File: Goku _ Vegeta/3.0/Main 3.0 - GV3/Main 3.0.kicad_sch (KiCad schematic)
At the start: 28 parts, among them J11 Motor Driver Inputs, J12 OpenMV H7, J13 Conn_01x04_Male, J15 Motor Driver 1 Power, J16 Motor Driver 2 Power, J23 Line PCB 2, J24 B3B-XH-A(LF)(SN), J25 Conn_01x02_Male, J5 XT60-M, J6 Voltmeter, J7 XT60-M, J8 XT60-M, J9 Line PCB 1, U1 DC-DC_Buck_Converter_7-24V_to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, U2 DEV-16771, U4 Adafruit_BNO055_STEMMA_QT

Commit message: Line 3.0 SCH 1st draft done + started working on SCH for main 3.0
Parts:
- removed C1, C3, C4: 10UF, Capacitor_SMD:C_0805_2012Metric, symbol Device:C_Small
- removed J11: Motor Driver Inputs, Box IDC header 2x5:Box IDC header 2x5, symbol Box IDC header 2x5:2-1761603-3
- removed J12: OpenMV H7, Box IDC header 2x3:Box IDC header 2x3, symbol Box IDC header 2x3:2-1761679-1
- removed J15: Motor Driver 1 Power, 5mm Pitch 2-Pin Screw Terminal Block:5mm Pitch 2-Pin Screw Terminal Block, symbol 5mm Pitch 2-Pin Screw Terminal Block:691137710002
- removed J16: Motor Driver 2 Power, 5mm Pitch 2-Pin Screw Terminal Block:5mm Pitch 2-Pin Screw Terminal Block, symbol 5mm Pitch 2-Pin Screw Terminal Block:691137710002
- removed J23: Line PCB 2, Box IDC header 2x3:Box IDC header 2x3, symbol Box IDC header 2x3:2-1761679-1
- removed J24: B3B-XH-A(LF)(SN), JST_B3B-XH-A(LF)(SN), symbol B3B-XH-A_LF__SN_:B3B-XH-A(LF)(SN)
- removed J5, J7, J8: XT60-M, XT60-M:XT60-M, symbol XT60-M:XT60-M
- removed J9: Line PCB 1, Box IDC header 2x3:Box IDC header 2x3, symbol Box IDC header 2x3:2-1761679-1
- removed U1: DC-DC_Buck_Converter_7-24V_to_5V_4A, 2.3 PCBs:DC-DC_Buck_Converter_7-24V_to_5V_4A, symbol DC-DC Buck Converter 7-24V to 5V 4A:DC-DC_Buck_Converter_7-24V_to_5V_4A
- removed U2: DEV-16771, MODULE_DEV-16771, symbol DEV-16771:DEV-16771
- added C1, C2: 10uF, Capacitor_SMD:C_0805_2012Metric, symbol Device:C_Polarized_Small
- added C3, C4: 0.1uF, Capacitor_SMD:C_0805_2012Metric, symbol Device:C_Polarized_Small
- added C5, C6: 3.3nF, Capacitor_SMD:C_0805_2012Metric, symbol Device:C_Polarized_Small
- added C7, C8: 22uF, Capacitor_SMD:C_0805_2012Metric, symbol Device:C_Polarized_Small
- added D1: LED, symbol Device:LED
- added D2, D3: STTH2002G-TR, Package_TO_SOT_SMD:TO-263-2, symbol Diode:STTH2002G
- added J1: Battery Buzzer 1, Connector_PinSocket_2.54mm:PinSocket_1x08_P2.54mm_Vertical, symbol Connector:Conn_01x08_Pin
- added J10: Power Switch, Connector_AMASS:AMASS_XT60-F_1x02_P7.20mm_Vertical, symbol Connector_Generic:Conn_01x02
- added J11: LEFT HEADERS, Connector_PinHeader_2.54mm:PinHeader_1x24_P2.54mm_Vertical, symbol Connector:Conn_01x24_Female
- added J14: RIGHT HEADERS, Connector_PinHeader_2.54mm:PinHeader_1x24_P2.54mm_Vertical, symbol Connector:Conn_01x24_Female
- added J2: Battery Buzzer 2, Connector_PinSocket_2.54mm:PinSocket_1x08_P2.54mm_Vertical, symbol Connector:Conn_01x08_Pin
- added J3: Battery Balance 1, Connector_JST:JST_XH_B3B-XH-A_1x03_P2.50mm_Vertical, symbol Connector:Conn_01x03_Socket
- added J4: Battery Balance 2, Connector_JST:JST_XH_B3B-XH-A_1x03_P2.50mm_Vertical, symbol Connector:Conn_01x03_Socket
- added J5: Battery 1, Connectors:DEANS, symbol Connector_Generic:Conn_01x02
- added J7: Battery 2, Connectors:DEANS, symbol Connector_Generic:Conn_01x02
- added J8: B-B PWR, Connector_AMASS:AMASS_XT60-F_1x02_P7.20mm_Vertical, symbol Connector_Generic:Conn_01x02
- added J9: I2C TO SLAVE, Connector_JST:JST_XH_B4B-XH-AM_1x04_P2.50mm_Vertical, symbol Connector:Conn_01x04_Male
- added L1, L2: 2.2uH, symbol Device:L
- added Q1: Q_Photo_NPN, symbol Device:Q_Photo_NPN
- added R1, R2: 100K, Resistor_SMD:R_0805_2012Metric, symbol Device:R_Small
- added R3: 95R, Resistor_SMD:R_0805_2012Metric, symbol Device:R_Small
- added R4, R5: 10K, Resistor_SMD:R_0805_2012Metric, symbol Device:R_Small
- added SW1: SW_DIP_x04, Button_Switch_THT:SW_DIP_SPSTx04_Slide_9.78x12.34mm_W7.62mm_P2.54mm, symbol Switch:SW_DIP_x04
- added U1: DEV-16771, DEV-16771:MODULE_DEV-16771, symbol DEV-16771:DEV-16771
- added U2: TPS62132, Package_DFN_QFN:VQFN-16-1EP_3x3mm_P0.5mm_EP1.68x1.68mm_ThermalVias, symbol Regulator_Switching:TPS62132
- added U3: TPS62133, Package_DFN_QFN:VQFN-16-1EP_3x3mm_P0.5mm_EP1.68x1.68mm_ThermalVias, symbol Regulator_Switching:TPS62133
- J13: value Conn_01x04_Male -> UART TO CAM; footprint (none) -> Connector_JST:JST_XH_B4B-XH-AM_1x04_P2.50mm_Vertical
- J25: footprint (none) -> Connector_JST:JST_XH_B2B-XH-A_1x02_P2.50mm_Vertical
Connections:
- net +15V: now also D2.3 (A), D3.3 (A), J10.2 (Pin_2), J8.1 (Pin_1)
- net +5V: now also C8.1, J14.1 (Pin_1), L2.2, Q1.1 (C), R2.2, R3.1, U1.5V, U1.VIN, U3.14 (VOS)
- net GND: now also J13.4 (Pin_4), C1.2, C3.2, C5.1, C7.2, C8.2, D1.1 (K), J11.1 (Pin_1), J14.15 (Pin_15), J14.2 (Pin_2), J7.1 (Pin_1), J8.2 (Pin_2), J9.4 (Pin_4), R4.2, R5.2, U1.GND1 (GND), U1.GND2 (GND__1), U1.GND3 (GND__2), U1.GND4 (GND__3), U1.GND5 (GND__4), U1.USB_GND1 (USB_GND), U1.USB_GND2 (USB_GND__1), U2.15 (PGND), U2.16 (PGND), U2.17 (EP), U2.5 (FB), U2.6 (AGND), U2.7 (FSW), U2.8 (DEF), U3.15 (PGND), U3.16 (PGND), U3.17 (EP), U3.5 (FB); no longer J13.2 (Pin_2)
- net LOGIC_SWTICH: now also R5.1
- net RST renamed 33
- net 33: now also J14.24 (Pin_24), U1.33 (MCLK2)
- net RX renamed 0
- net 0: now also J13.3 (Pin_3), J11.2 (Pin_2), U1.0 (RX1)
- net SCL renamed 19
- net 19: now also J14.8 (Pin_8), J9.3 (Pin_3), U1.19 (A5); no longer J13.3 (Pin_3)
- net SDA renamed 18
- net 18: now also J14.9 (Pin_9), J9.2 (Pin_2), U1.18 (A4); no longer J13.4 (Pin_4)
- net TX renamed 1
- net 1: now also J13.2 (Pin_2), J11.3 (Pin_3), U1.1 (TX1)
- new net: L1.1, U2.1 (SW), U2.2 (SW), U2.3 (SW)
- new net: C1.1, C3.1, D2.2 (K), U2.10 (AVIN), U2.11 (PVIN), U2.12 (PVIN), U2.13 (EN)
- new net: R1.1, U2.4 (PG)
- new net: C5.2, U2.9 (SS/TR)
- new net: L2.1, U3.1 (SW), U3.2 (SW), U3.3 (SW)
- new net: D1.2 (A), R3.2
- new net: J5.1 (Pin_1), J7.2 (Pin_2)
- new net: J1.3 (Pin_3), J3.1 (Pin_1)
- new net: J1.2 (Pin_2), J3.2 (Pin_2)
- new net: J1.1 (Pin_1), J3.3 (Pin_3)
- new net: C2.1, C4.1, D3.2 (K), U3.10 (AVIN), U3.11 (PVIN), U3.12 (PVIN), U3.13 (EN)
- new net: R2.1, U3.4 (PG)
- new net: C2.2, C4.2, C6.1, U3.6 (AGND), U3.7 (FSW), U3.8 (DEF)
- new net: C6.2, U3.9 (SS/TR)
- new net: J10.1 (Pin_1), J5.2 (Pin_2)
- new net: J2.1 (Pin_1), J4.3 (Pin_3)
- new net: J2.2 (Pin_2), J4.2 (Pin_2)
- new net: J2.3 (Pin_3), J4.1 (Pin_1)
- new net +3V3: C7.1, J11.15 (Pin_15), J14.3 (Pin_3), L1.2, R1.2, SW1.1, SW1.2, SW1.3, SW1.4, U2.14 (VOS)
- new net 10: J11.12 (Pin_12), U1.10 (CS1)
- new net 11: J11.13 (Pin_13), U1.11 (MOSI)
- new net 12: J11.14 (Pin_14), U1.12 (MISO)
- new net 13: J14.14 (Pin_14), U1.13 (SCK)
- new net 14: J14.13 (Pin_13), U1.14 (A0)
- new net 15: J14.12 (Pin_12), U1.15 (A1)
- new net 16: J14.11 (Pin_11), U1.16 (A2)
- new net 17: J14.10 (Pin_10), U1.17 (A3)
- new net 2: J11.4 (Pin_4), U1.2 (OUT2)
- new net 20: J14.7 (Pin_7), U1.20 (A6)
- new net 21: J14.6 (Pin_6), U1.21 (A7)
- new net 22: J14.5 (Pin_5), U1.22 (A8)
- new net 23: J14.4 (Pin_4), U1.23 (A9)
- new net 24: J11.16 (Pin_16), Q1.2 (E), R4.1, U1.24 (A10)
- new net 25: J11.17 (Pin_17), U1.25 (A11)
- new net 26: J11.18 (Pin_18), U1.26 (A12)
- new net 27: J11.19 (Pin_19), U1.27 (A13)
- new net 28: J11.20 (Pin_20), SW1.6, U1.28 (RX7)
- new net 29: J11.21 (Pin_21), SW1.5, U1.29 (TX7)
- new net 3: J11.5 (Pin_5), U1.3 (LRCLK2)
- new net 30: J11.22 (Pin_22), U1.30 (CRX3)
- new net 31: J11.23 (Pin_23), U1.31 (CTX3)
- new net 32: J11.24 (Pin_24), J9.1 (Pin_1), U1.32 (OUT1B)
- new net 34: J14.23 (Pin_23), U1.34 (RX8)
- new net 35: J14.22 (Pin_22), U1.35 (TX8)
- new net 36: J14.21 (Pin_21), U1.36 (CS2)
- new net 37: J14.20 (Pin_20), U1.37 (CS3)
- new net 38: J14.19 (Pin_19), U1.38 (A14)
- new net 39: J14.18 (Pin_18), U1.39 (A15)
- new net 4: J11.6 (Pin_6), U1.4 (BCLK2)
- new net 40: J14.17 (Pin_17), U1.40 (A16)
- new net 41: J14.16 (Pin_16), U1.41 (A17)
- new net 5: J11.7 (Pin_7), U1.5 (IN2)
- new net 6: J11.8 (Pin_8), U1.6 (OUT1D)
- new net 7: J11.9 (Pin_9), SW1.8, U1.7 (RX2)
- new net 8: J11.10 (Pin_10), SW1.7, U1.8 (TX2)
- new net 9: J11.11 (Pin_11), U1.9 (OUT1C)
- no-connect marks 7 -> 29
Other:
- note added: "3V3 POWER RAIL - LEDs and Phototransistors"
- note added: "5V POWER RAIL - Microcontroller"
- note added: "LINE BREAK CIRCUIT"
- note added: "MCU"
- note added: "POWER SUPPLY"
- note added: "double check polarity of connections"
- note removed: "Battery 1"
- note removed: "Battery 2"
- note removed: "Power Switch"
- moved on the sheet: J6, R13, R14, TP1, TP2, TP3, TP4, TP5, TP6

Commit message: LINE 3.0 Update
-Updated to have caps on power rails
-imrpoves tolerance of 100uf capacitor
-main power cable went from xt60 to xt30
- remove outer wheel guard
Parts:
- removed C3, C4: 0.1uF, Capacitor_SMD:C_0805_2012Metric, symbol Device:C_Polarized_Small
- removed C5, C6: 3.3nF, Capacitor_SMD:C_0805_2012Metric, symbol Device:C_Polarized_Small
- removed C7, C8: 22uF, Capacitor_SMD:C_0805_2012Metric, symbol Device:C_Polarized_Small
- removed D2, D3: STTH2002G-TR, Package_TO_SOT_SMD:TO-263-2, symbol Diode:STTH2002G
- removed J10: Power Switch, Connector_AMASS:AMASS_XT60-F_1x02_P7.20mm_Vertical, symbol Connector_Generic:Conn_01x02
- removed J11: LEFT HEADERS, Connector_PinHeader_2.54mm:PinHeader_1x24_P2.54mm_Vertical, symbol Connector:Conn_01x24_Female
- removed J13: UART TO CAM, Connector_JST:JST_XH_B4B-XH-AM_1x04_P2.50mm_Vertical, symbol Connector:Conn_01x04_Male
- removed J14: RIGHT HEADERS, Connector_PinHeader_2.54mm:PinHeader_1x24_P2.54mm_Vertical, symbol Connector:Conn_01x24_Female
- removed J5: Battery 1, Connectors:DEANS, symbol Connector_Generic:Conn_01x02
- removed J7: Battery 2, Connectors:DEANS, symbol Connector_Generic:Conn_01x02
- removed J8: B-B PWR, Connector_AMASS:AMASS_XT60-F_1x02_P7.20mm_Vertical, symbol Connector_Generic:Conn_01x02
- removed J9: I2C TO SLAVE, Connector_JST:JST_XH_B4B-XH-AM_1x04_P2.50mm_Vertical, symbol Connector:Conn_01x04_Male
- removed L1, L2: 2.2uH, symbol Device:L
- removed SW1: SW_DIP_x04, Button_Switch_THT:SW_DIP_SPSTx04_Slide_9.78x12.34mm_W7.62mm_P2.54mm, symbol Switch:SW_DIP_x04
- removed TP1: TestPoint - 5V, TestPoint:TestPoint_THTPad_D2.0mm_Drill1.0mm, symbol Connector:TestPoint
- removed TP18: LOGIC_SWITCH, TestPoint:TestPoint_THTPad_D2.0mm_Drill1.0mm, symbol Connector:TestPoint
- removed TP2: TestPoint - SCL, TestPoint:TestPoint_THTPad_D2.0mm_Drill1.0mm, symbol Connector:TestPoint
- removed TP3: TestPoint - SDA, TestPoint:TestPoint_THTPad_D2.0mm_Drill1.0mm, symbol Connector:TestPoint
- removed TP4: TestPoint - TX, TestPoint:TestPoint_THTPad_D2.0mm_Drill1.0mm, symbol Connector:TestPoint
- removed TP5: TestPoint - RX, TestPoint:TestPoint_THTPad_D2.0mm_Drill1.0mm, symbol Connector:TestPoint
- removed TP6: TestPoint - GND, TestPoint:TestPoint_THTPad_D2.0mm_Drill1.0mm, symbol Connector:TestPoint
- removed U1: DEV-16771, DEV-16771:MODULE_DEV-16771, symbol DEV-16771:DEV-16771
- removed U2: TPS62132, Package_DFN_QFN:VQFN-16-1EP_3x3mm_P0.5mm_EP1.68x1.68mm_ThermalVias, symbol Regulator_Switching:TPS62132
- removed U3: TPS62133, Package_DFN_QFN:VQFN-16-1EP_3x3mm_P0.5mm_EP1.68x1.68mm_ThermalVias, symbol Regulator_Switching:TPS62133
- added J10, J13, J17, J18, J19: Conn_01x02_Male, Connector_JST:JST_XH_B2B-XH-A_1x02_P2.50mm_Vertical, symbol Connector:Conn_01x02_Male
- added J11: BATTERY POWER, Connector_AMASS:AMASS_XT30U-F_1x02_P5.0mm_Vertical, symbol Connector:Conn_01x02_Male
- added J12: RIGHT HEADERS, Connector_PinHeader_2.54mm:PinHeader_1x24_P2.54mm_Vertical, symbol Connector:Conn_01x24_Female
- added J14: BACKUP 5V, Connector_AMASS:AMASS_XT30U-F_1x02_P5.0mm_Vertical, symbol Connector:Conn_01x02_Male
- added J15: BACKUP 3V3, Connector_AMASS:AMASS_XT30U-F_1x02_P5.0mm_Vertical, symbol Connector:Conn_01x02_Male
- added J16: I2C, Connector_AMASS:AMASS_XT30U-F_1x02_P5.0mm_Vertical, symbol Connector:Conn_01x02_Male
- added J20: I2C, symbol Connector:Conn_01x03_Socket
- added J21: SPI, symbol Connector:Conn_01x05_Socket
- added J22: UART, symbol Connector:Conn_01x03_Socket
- added J5: Power Switch, Connector_AMASS:AMASS_XT30UPB-F_1x02_P5.0mm_Vertical, symbol Connector:Conn_01x02_Pin
- added J7: LEFT HEADERS, Connector_PinHeader_2.54mm:PinHeader_1x24_P2.54mm_Vertical, symbol Connector:Conn_01x24_Female
- added J8: MID HEADERS, Connector_PinHeader_2.54mm:PinHeader_1x05_P2.54mm_Vertical, symbol Connector:Conn_01x05_Socket
- added J9: 4S Battery, Connector_AMASS:AMASS_XT60-M_1x02_P7.20mm_Vertical, symbol Connector:Conn_01x02_Pin
- added R10, R6, R7, R8, R9: 10K, Resistor_SMD:R_0805_2012Metric, symbol Device:R_Small
- added U5: DEV-16771, DEV-16771:MODULE_DEV-16771, symbol DEV-16771:DEV-16771
- added U6, U7: ~, Converter_DCDC:DC-DC Multi-output Buck Converter, symbol Converter_DCDC:DC-DC_Multi-output_Buck_Converter
- C1, C2: value 10uF -> 100uF; footprint Capacitor_SMD:C_0805_2012Metric -> Capacitor_THT:CP_Radial_D10.0mm_P5.00mm
- R1, R2: value 100K -> 10K
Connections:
- net +15V: now also J11.2 (Pin_2), J5.1 (Pin_1), U6.2 (IN+), U7.2 (IN+)
- net +3V3: now also C1.2, C2.2, J25.1 (Pin_1), R13.2, R14.2, J10.1 (Pin_1), J12.3 (Pin_3), J13.1 (Pin_1), J15.2 (Pin_2), J17.1 (Pin_1), J18.1 (Pin_1), J19.1 (Pin_1), J7.15 (Pin_15), R10.2, R9.2, U6.4 (OUT+), U7.4 (OUT+); no longer R1.2
- net +5V: now also J12.1 (Pin_1), J14.2 (Pin_2), U5.5V, U5.VIN; no longer J25.1 (Pin_1), R13.2, R14.2, R2.2
- net 0: now also J22.1 (Pin_1), J7.2 (Pin_2), U5.0 (RX1)
- net 1: now also J22.2 (Pin_2), J7.3 (Pin_3), U5.1 (TX1)
- net 10: now also J21.4 (Pin_4), J7.12 (Pin_12), U5.10 (CS1)
- net 11: now also J21.3 (Pin_3), J7.13 (Pin_13), U5.11 (MOSI)
- net 12: now also J21.2 (Pin_2), J7.14 (Pin_14), U5.12 (MISO)
- net 13: now also J12.14 (Pin_14), J21.1 (Pin_1), U5.13 (SCK)
- net 14: now also J12.13 (Pin_13), U5.14 (A0)
- net 15: now also J12.12 (Pin_12), U5.15 (A1)
- net 16: now also J12.11 (Pin_11), U5.16 (A2)
- net 17: now also J12.10 (Pin_10), U5.17 (A3)
- net 18: now also J12.9 (Pin_9), J16.2 (Pin_2), J20.2 (Pin_2), U5.18 (A4); no longer U4.5 (SDA)
- net 19: now also J12.8 (Pin_8), J16.1 (Pin_1), J20.1 (Pin_1), U5.19 (A5); no longer U4.4 (SCL)
- net 2: now also J7.4 (Pin_4), U5.2 (OUT2)
- net 20: now also J12.7 (Pin_7), U5.20 (A6)
- net 21: now also J12.6 (Pin_6), U5.21 (A7)
- net 22: now also J12.5 (Pin_5), U5.22 (A8)
- net 23: now also J12.4 (Pin_4), U5.23 (A9)
- net 24: now also J7.16 (Pin_16), U5.24 (A10); no longer Q1.2 (E), R4.1
- net 25: now also J7.17 (Pin_17), U5.25 (A11)
- net 26: now also J7.18 (Pin_18), U5.26 (A12)
- net 27: now also J7.19 (Pin_19), U5.27 (A13)
- net 28: now also J7.20 (Pin_20), U5.28 (RX7)
- net 29: now also J7.21 (Pin_21), U5.29 (TX7)
- net 3: now also J7.5 (Pin_5), U5.3 (LRCLK2)
- net 30: now also J7.22 (Pin_22), U5.30 (CRX3)
- net 31: now also J7.23 (Pin_23), U5.31 (CTX3)
- net 32: now also J7.24 (Pin_24), U5.32 (OUT1B)
- net 33: now also J12.24 (Pin_24), U5.33 (MCLK2); no longer U4.6 (RST)
- net 34: now also J12.23 (Pin_23), U5.34 (RX8)
- net 35: now also J12.22 (Pin_22), U5.35 (TX8)
- net 36: now also J12.21 (Pin_21), U5.36 (CS2)
- net 37: now also J12.20 (Pin_20), U5.37 (CS3)
- net 38: now also J12.19 (Pin_19), U5.38 (A14)
- net 39: now also J12.18 (Pin_18), U5.39 (A15)
- net 4: now also J7.6 (Pin_6), U5.4 (BCLK2)
- net 40: now also J12.17 (Pin_17), U5.40 (A16)
- net 41: now also J12.16 (Pin_16), U5.41 (A17)
- net 5: now also J7.7 (Pin_7), U5.5 (IN2)
- net 6: now also J7.8 (Pin_8), U5.6 (OUT1D)
- net 7: now also J7.9 (Pin_9), U5.7 (RX2)
- net 8: now also J7.10 (Pin_10), U5.8 (TX2)
- net 9: now also J7.11 (Pin_11), U5.9 (OUT1C)
- net GND: now also C1.1, C2.1, R1.2, R2.2, J11.1 (Pin_1), J12.15 (Pin_15), J12.2 (Pin_2), J14.1 (Pin_1), J15.1 (Pin_1), J20.3 (Pin_3), J21.5 (Pin_5), J22.3 (Pin_3), J7.1 (Pin_1), J8.3 (Pin_3), J9.2 (Pin_2), R6.2, R7.2, R8.2, U5.GND1 (GND), U5.GND2 (GND__1), U5.GND3 (GND__2), U5.GND4 (GND__3), U5.GND5 (GND__4), U5.USB_GND1 (USB_GND), U5.USB_GND2 (USB_GND__1), U6.1 (IN-), U6.3 (OUT-), U7.1 (IN-), U7.3 (OUT-); no longer C1.2
- net SW2: now reaches R1.1
- net SW2: now also J17.2 (Pin_2)
- net SW3: now reaches R2.1
- net SW3: now also J18.2 (Pin_2)
- net LOGIC_SWTICH renamed SW1
- new net: J5.2 (Pin_2), J9.1 (Pin_1)
- new net LINE BREAK: Q1.2 (E), R4.1
- new net ON/OFF: J8.1 (Pin_1), U5.ON/OFF
- new net PROGRAM: J8.2 (Pin_2), U5.PROGRAM
- new net RST: U4.6 (RST)
- new net SCL1: R9.1, U4.4 (SCL)
- new net SDA1: R10.1, U4.5 (SDA)
- new net SW4: J19.2 (Pin_2), R6.1
- new net SW5: J10.2 (Pin_2), R7.1
- new net SW6: J13.2 (Pin_2), R8.1
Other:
- note added: "3V3 POWER RAIL"
- note added: "5V POWER RAIL"
- note added: "BATTERY"
- note added: "CAM BUS(s)"
- note added: "CONN TO LINE"
- note added: "LOGIC SWITCHES"
- note added: "SENSORS"
- note removed: "3V3 POWER RAIL - LEDs and Phototransistors"
- note removed: "5V POWER RAIL - Microcontroller"
- note removed: "double check polarity of connections"
- moved on the sheet: D1, J1, J25, J3, J4, J6, Q1, R13, R14, R3, R4, R5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

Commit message: move to 3.1
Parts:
- removed J2: Battery Buzzer 2, Connector_PinSocket_2.54mm:PinSocket_1x08_P2.54mm_Vertical, symbol Connector:Conn_01x08_Pin
- added J5: Battery Buzzer 2, Connector_PinSocket_2.54mm:PinSocket_1x08_P2.54mm_Vertical, symbol Connector:Conn_01x08_Pin
- D1, Q1: footprint (none) -> 5mm Pitch 2-Pin Screw Terminal Block:5mm Pitch 2-Pin Screw Terminal Block
- J12: renamed from J21; footprint (none) -> Connector_PinSocket_2.54mm:PinSocket_1x05_P2.54mm_Vertical
- J13: renamed from J22; footprint (none) -> Connector_PinSocket_2.54mm:PinSocket_1x03_P2.54mm_Vertical
- J14: renamed from J20; footprint (none) -> Connector_PinSocket_2.54mm:PinSocket_1x04_P2.54mm_Vertical
- renumbered J9 to J1, J15 to J10, J16 to J11, J25 to J15, J17 to J16, J18 to J17, J19 to J18, J10 to J19, J5 to J2, J13 to J20, J7 to J21, J8 to J22, J12 to J23, J6 to J3, J1 to J4, J3 to J6, J4 to J7, J11 to J8, J14 to J9, R13 to R1, R6 to R10, R7 to R11, R8 to R12, R14 to R2, R9 to R3, R10 to R4, R3 to R5, R4 to R6, R5 to R7, R1 to R8, R2 to R9, U6 to U1, U7 to U2, U4 to U3, U5 to U4
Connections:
- net at J7.3 (Pin_3): now also J5.1 (Pin_1)
- net at J7.2 (Pin_2): now also J5.2 (Pin_2)
- net at J7.1 (Pin_1): now also J5.3 (Pin_3)
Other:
- moved on the sheet: J4, J6, J7

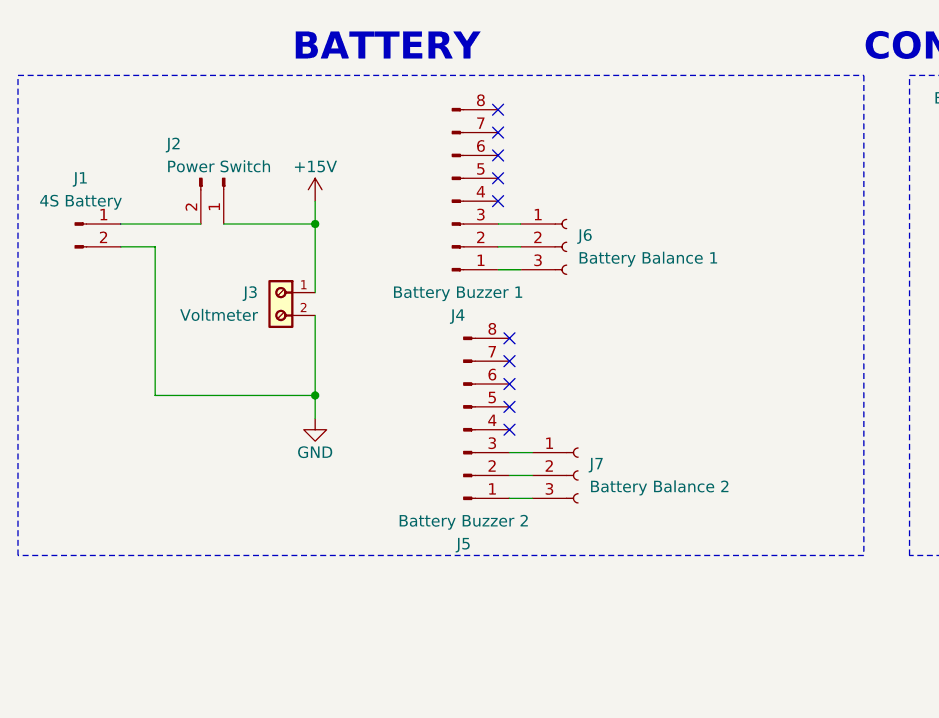
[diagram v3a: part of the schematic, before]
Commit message: MAIN 3.1 DONE no silkscreen
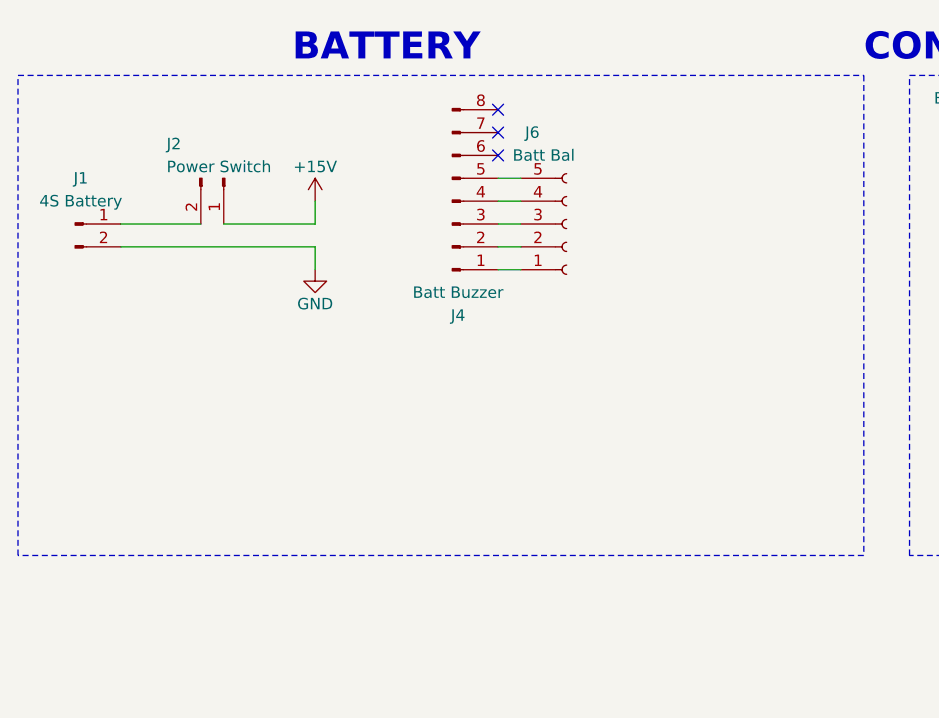
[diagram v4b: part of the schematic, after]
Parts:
- removed J3: Voltmeter, 5mm Pitch 2-Pin Screw Terminal Block:5mm Pitch 2-Pin Screw Terminal Block, symbol 5mm Pitch 2-Pin Screw Terminal Block:691137710002
- removed J5: Battery Buzzer 2, Connector_PinSocket_2.54mm:PinSocket_1x08_P2.54mm_Vertical, symbol Connector:Conn_01x08_Pin
- removed J6: Battery Balance 1, Connector_JST:JST_XH_B3B-XH-A_1x03_P2.50mm_Vertical, symbol Connector:Conn_01x03_Socket
- removed J7: Battery Balance 2, Connector_JST:JST_XH_B3B-XH-A_1x03_P2.50mm_Vertical, symbol Connector:Conn_01x03_Socket
- added J6: Batt Bal, symbol Connector:Conn_01x05_Socket
- J4: value Battery Buzzer 1 -> Batt Buzzer
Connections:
- net at J4.3 (Pin_3): now also J6.3 (Pin_3)
- net at J4.2 (Pin_2): now also J6.2 (Pin_2)
- net at J4.1 (Pin_1): now also J6.1 (Pin_1)
- net at J4.4 (Pin_4): now also J6.4 (Pin_4)
- net at J4.5 (Pin_5): now also J6.5 (Pin_5)
- no-connect marks 29 -> 22
